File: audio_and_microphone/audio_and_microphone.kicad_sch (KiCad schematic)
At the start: 29 parts, among them J2 Conn_01x02, U1 LM4810, U2 ${SIM.PARAMS}, U3 ${SIM.PARAMS}

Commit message: cleaned filed to merge microphone and audio schematics into audio_and_microphone schematic
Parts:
- added V1: VSIN, symbol Simulation_SPICE:VSIN
- added V1: 3.3, symbol Simulation_SPICE:VDC
- added V3: VPWL, symbol Simulation_SPICE:VPWL
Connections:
- net +3V3: now also V1.1
- net 226 Hz: now also V1.1
- net GND: now also V1.2, V1.2, V3.2
- net PWM_VOL: now also V3.1
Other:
- moved on the sheet: C11, C12, C13, C16, C21, C24, C25, C28, J2, R20, R21, R23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

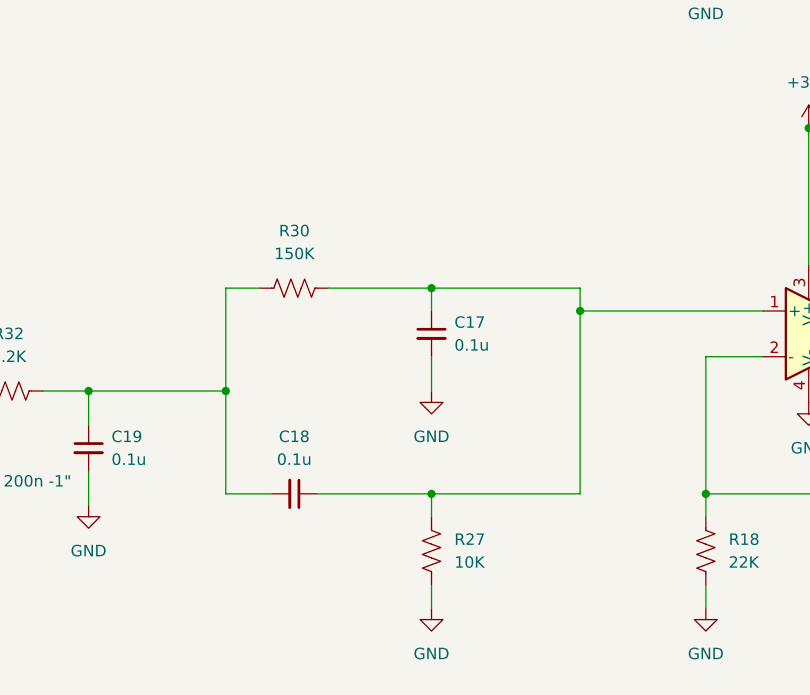
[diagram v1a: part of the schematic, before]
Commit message: updated audio and microphone circuit with new redesigned notch filter that was lost
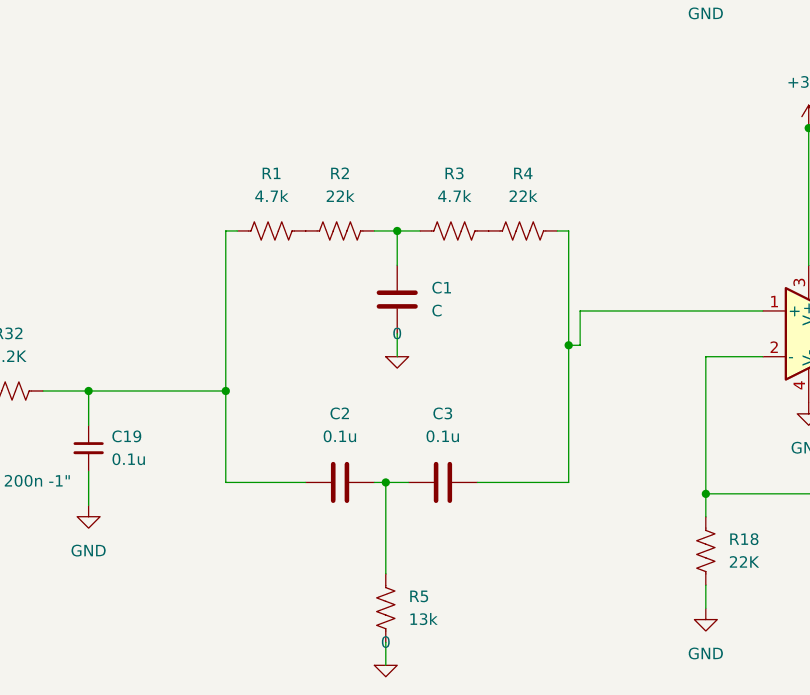
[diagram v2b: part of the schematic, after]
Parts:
- removed C17, C18: 0.1u, symbol Device:C_Small
- removed R27: 10K, symbol Device:R_US
- removed R30: 150K, symbol Device:R_US
- added C1: C, symbol Device:C
- added C2, C3: 0.1u, symbol Device:C
- added R1, R3: 4.7k, symbol Device:R_US
- added R2, R4: 22k, symbol Device:R_US
- added R5: 13k, symbol Device:R_US
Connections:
- net at U2.1 (+): now also C3.2, R4.2
- net at C19.1, R32.1: now also C2.1, R1.1
- new net: C2.2, C3.1, R5.1
- new net: R1.2, R2.1
- new net: C1.1, R2.2, R3.1
- new net: R3.2, R4.1
- new net 0: C1.2, R5.2
